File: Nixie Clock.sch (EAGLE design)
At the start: 46 parts, among them T0 MPSA42, T1 MPSA42, T10 MPSA42, T11 MPSA42, T12 MPSA42, T13 MPSA42, T14 MPSA42, T15 MPSA42, T16 MPSA42, T17 MPSA42, T18 MPSA42, T19 MPSA42, T2 MPSA42, T3 MPSA42, T4 MPSA42, T5 MPSA42, T6 MPSA42, T7 MPSA42, T8 MPSA42, T9 MPSA42

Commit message: Create 'Nixie Clock' and delete previous attempts with tubes
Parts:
- removed HOURS: (no value), con-harting:CON20
- removed HOURS_D, HOURS_U: IN-14, russian-nixies:IN-14
- removed POWER_SUPPLY: CON_2_SIL, PGT:CON_2_SIL
- added CON_LOGIC_POWER, CON_TUBE_POWER: CON_2_SIL, PGT:CON_2_SIL
- added HOURS_TENS, HOURS_UNITS, MINUTES_TENS, MINUTES_UNITS, SECONDS_TENS, SECONDS_UNITS: IN-14, russian-nixies:IN-14
- added R23, R24, R25, R26, R27, R28, R29, R30, R31, R32, R33, R34, R35, R36, R39, R40, R41, R42, R43, R44, R45, R46, R47, R48, R49, R50, R54: 33.3k, resistor:R-EU_0207/10
- added R37, R38: (no value), resistor:R-EU_0207/10
- added T20, T21, T22, T23, T24, T25, T26, T27, T28, T29, T30, T31, T32, T33, T34, T35, T36, T37, T38, T39, T40, T41, T42, T43, T44: MPSA42, PGT:MPSA42
- R10, R11, R12, R13, R14, R15, R16, R17, R18, R21, R22, R3, R4, R5, R6, R7, R8, R9: value (none) -> 33.3k
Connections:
- removed net DIGIT_D0: HOURS.10, R22.1
- removed net DIGIT_D1: HOURS.12, R13.1
- removed net DIGIT_D2: HOURS.14, R14.1
- removed net DIGIT_D3: HOURS.16, R15.1
- removed net DIGIT_D4: HOURS.18, R16.1
- removed net DIGIT_D5: HOURS.20, R17.1
- removed net DIGIT_D6: HOURS.2, R18.1
- removed net DIGIT_D7: HOURS.4, R19.1
- removed net DIGIT_D8: HOURS.6, R20.1
- removed net DIGIT_D9: HOURS.8, R21.1
- removed net DIGIT_U0: HOURS.9, R12.1
- removed net DIGIT_U1: HOURS.11, R3.1
- removed net DIGIT_U2: HOURS.13, R4.1
- removed net DIGIT_U3: HOURS.15, R5.1
- removed net DIGIT_U4: HOURS.17, R6.1
- removed net DIGIT_U5: HOURS.19, R7.1
- removed net DIGIT_U6: HOURS.1, R8.1
- removed net DIGIT_U7: HOURS.3, R9.1
- removed net DIGIT_U8: HOURS.5, R10.1
- removed net DIGIT_U9: HOURS.7, R11.1
- removed net N$1 (its old number): HOURS_U.0, T0.C
- removed net N$13 (its old number): HOURS_U.8, T8.C
- removed net N$14 (its old number): HOURS_U.7, T7.C
- removed net N$16 (its old number): HOURS_U.5, T5.C
- removed net N$17 (its old number): HOURS_U.1, T1.C
- removed net N$18 (its old number): HOURS_U.4, T4.C
- removed net N$2 (its old number): HOURS_U.9, T9.C
- new net N$33: SECONDS_UNITS.9, T9.C
- new net N$37: R26.2, T21.B
- new net N$38: R27.2, T22.B
- new net N$39: R28.2, T23.B
- new net N$40: R29.2, T24.B
- new net N$43: MINUTES_TENS.A, R20.1
- new net N$44: R31.2, T27.B
- new net N$45: R32.2, T28.B
- new net N$46: R33.2, T29.B
- new net N$47: R34.2, T30.B
- new net N$48: R35.2, T31.B
- new net N$49: R36.2, T26.B
- new net N$50: R21.2, T16.B
- new net N$51: R22.2, T17.B
- new net N$52: R23.2, T18.B
- new net N$53: MINUTES_TENS.1, T27.C
- new net N$54: MINUTES_TENS.2, T28.C
- new net N$55: MINUTES_TENS.3, T29.C
- new net N$56: MINUTES_TENS.4, T30.C
- new net N$57: MINUTES_TENS.5, T31.C
- new net N$58: MINUTES_TENS.0, T26.C
- new net N$59: MINUTES_UNITS.1, T16.C
- new net N$60: MINUTES_UNITS.2, T17.C
- new net N$61: MINUTES_UNITS.3, T18.C
- new net N$62: MINUTES_UNITS.4, T19.C
- new net N$63: MINUTES_UNITS.5, T20.C
- new net N$64: MINUTES_UNITS.6, T21.C
- new net N$65: MINUTES_UNITS.0, T25.C
- new net N$66: MINUTES_UNITS.9, T24.C
- new net N$67: MINUTES_UNITS.8, T23.C
- new net N$68: R43.2, T36.B
- new net N$69: R44.2, T37.B
- new net N$70: R45.2, T38.B
- new net N$71: R46.2, T39.B
- new net N$72: R47.2, T40.B
- new net N$73: R48.2, T41.B
- new net N$74: HOURS_UNITS.A, R37.1
- new net N$75: HOURS_TENS.A, R38.1
- new net N$76: R49.2, T43.B
- new net N$77: R50.2, T44.B
- new net N$78: HOURS_TENS.0, T42.C
- new net N$8: R1.1, SECONDS_UNITS.A
- new net N$81: R54.2, T42.B
- new net N$82: R39.2, T32.B
- new net N$83: R40.2, T33.B
- new net N$84: R41.2, T34.B
- new net N$85: HOURS_TENS.1, T43.C
- new net N$86: HOURS_TENS.2, T44.C
- new net N$9: R2.1, SECONDS_TENS.A
- new net N$91: HOURS_UNITS.1, T32.C
- new net N$92: HOURS_UNITS.2, T33.C
- new net N$93: HOURS_UNITS.3, T34.C
- new net N$94: HOURS_UNITS.4, T35.C
- new net N$95: HOURS_UNITS.5, T36.C
- new net N$96: HOURS_UNITS.6, T37.C
- new net N$97: HOURS_UNITS.0, T41.C
- new net N$98: HOURS_UNITS.9, T40.C
- new net N$99: HOURS_UNITS.8, T39.C
- new net VHIGH: CON_TUBE_POWER.P$1, R1.2, R19.2, R2.2, R20.2, R37.2, R38.2
- net GND: now also CON_LOGIC_POWER.P$2, CON_TUBE_POWER.P$2, HOURS_UNITS.7, MINUTES_UNITS.7, SECONDS_UNITS.7, T20.E, T21.E, T22.E, T23.E, T24.E, T25.E, T26.E, T27.E, T28.E, T29.E, T30.E, T31.E, T32.E, T33.E, T34.E, T35.E, T36.E, T37.E, T38.E, T39.E, T40.E, T41.E, T42.E, T43.E, T44.E; no longer POWER_SUPPLY.P$2
- net N$15: now also R18.2, T10.B; no longer HOURS_U.6, T6.C
- net N$19: now also SECONDS_TENS.1, T11.C; no longer HOURS_U.2, T2.C
- net N$20: now also SECONDS_TENS.2, T12.C; no longer HOURS_D.0, T10.C
- net N$21: now also SECONDS_TENS.3, T13.C; no longer HOURS_U.3, T3.C
- net N$22: now also SECONDS_TENS.4, T14.C; no longer HOURS_D.9, T19.C
- net N$23: now also SECONDS_TENS.5, T15.C; no longer HOURS_U.A, R1.2
- net N$24: now also SECONDS_TENS.0, T10.C; no longer HOURS_D.8, T18.C
- net N$25: now also R42.2, T35.B; no longer HOURS_D.7, T17.C
- net N$26: now also SECONDS_UNITS.1, T1.C; no longer HOURS_D.6, T16.C
- net N$27: now also SECONDS_UNITS.2, T2.C; no longer HOURS_D.5, T15.C
- net N$28: now also SECONDS_UNITS.3, T3.C; no longer HOURS_D.2, T12.C
- net N$29: now also SECONDS_UNITS.4, T4.C; no longer HOURS_D.A, R2.2
- net N$30: now also SECONDS_UNITS.5, T5.C; no longer HOURS_D.3, T13.C
- net N$31: now also SECONDS_UNITS.6, T6.C; no longer HOURS_D.4, T14.C
- net N$32: now also SECONDS_UNITS.0, T0.C; no longer HOURS_D.1, T11.C
- net N$34: now also SECONDS_UNITS.8, T8.C; no longer R18.2, T16.B
- net N$35: now also R24.2, T19.B; no longer R19.2, T17.B
- net N$36: now also R25.2, T20.B; no longer R22.2, T10.B
- net N$41: now also R30.2, T25.B; no longer R20.2, T18.B
- net N$42: now also MINUTES_UNITS.A, R19.1; no longer R21.2, T19.B
- net VCC: now also CON_LOGIC_POWER.P$1; no longer POWER_SUPPLY.P$1, R1.1, R2.1

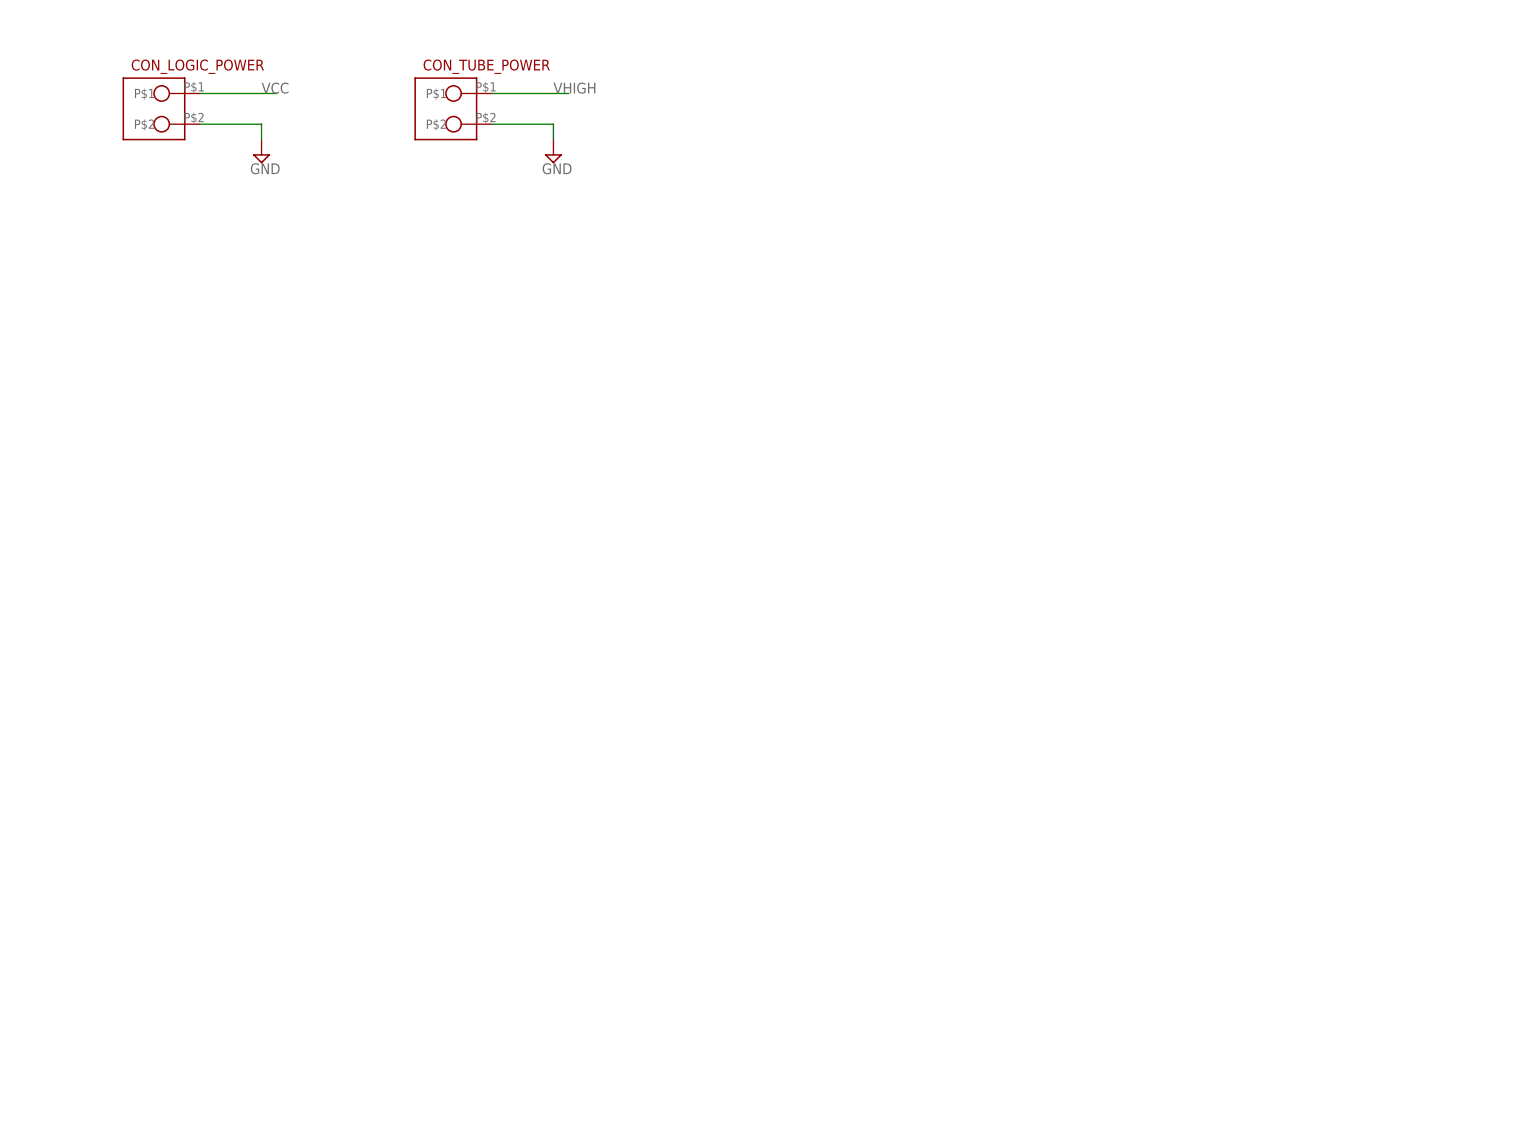
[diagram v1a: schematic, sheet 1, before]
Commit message: Uncompleted schematics for the Nixie Clock and simulation for AND with diodes
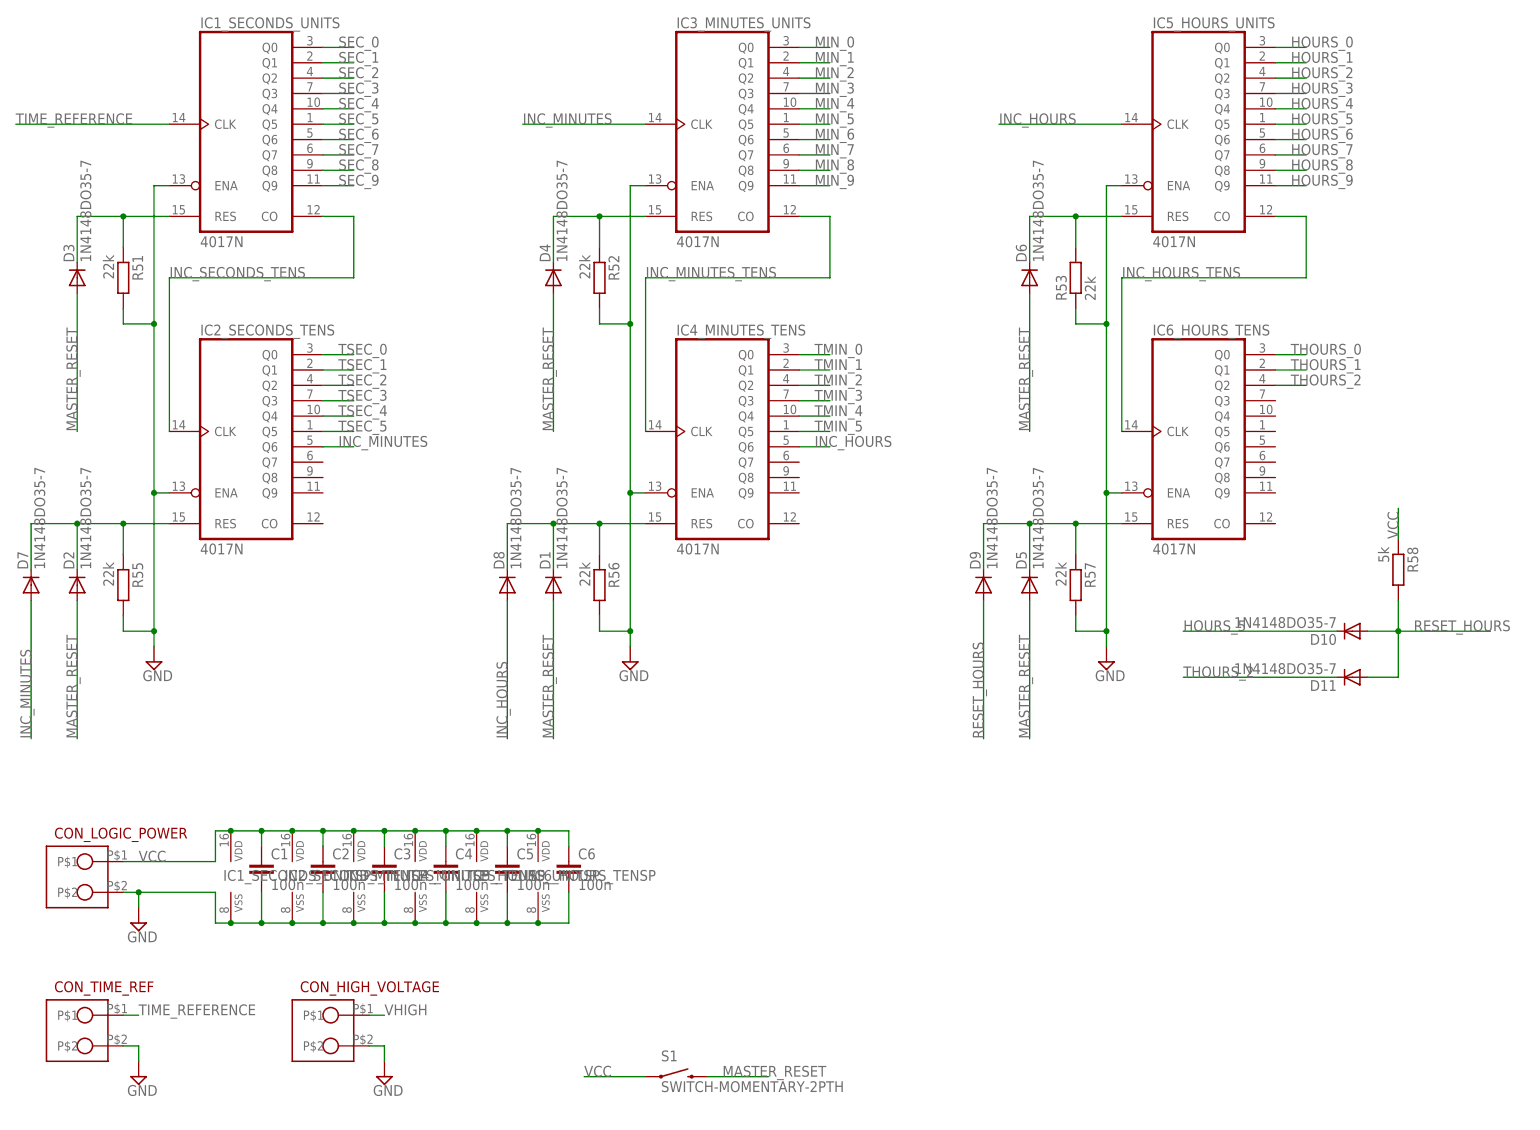
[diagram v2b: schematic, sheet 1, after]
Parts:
- removed CON_TUBE_POWER: CON_2_SIL, PGT:CON_2_SIL
- added C1, C2, C3, C4, C5, C6: 100n, resistor:C-EU050-030X075
- added CON_HIGH_VOLTAGE, CON_TIME_REF: CON_2_SIL, PGT:CON_2_SIL
- added D1, D10, D11, D2, D3, D4, D5, D6, D7, D8, D9: 1N4148DO35-7, diode:1N4148DO35-7
- added IC1_SECONDS_UNITS, IC2_SECONDS_TENS, IC3_MINUTES_UNITS, IC4_MINUTES_TENS, IC5_HOURS_UNITS, IC6_HOURS_TENS: 4017N, 40xx:4017N
- added R51, R52, R53, R55, R56, R57: 22k, resistor:R-EU_0207/10
- added R58: 5k, resistor:R-EU_0207/10
- added S1: SWITCH-MOMENTARY-2PTH, SparkFun-Electromechanical:SWITCH-MOMENTARY-2PTH
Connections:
- new net HOURS_0: IC5_HOURS_UNITSA.Q0, R48.1
- new net HOURS_1: IC5_HOURS_UNITSA.Q1, R39.1
- new net HOURS_2: IC5_HOURS_UNITSA.Q2, R40.1
- new net HOURS_3: IC5_HOURS_UNITSA.Q3, R41.1
- new net HOURS_4: IC5_HOURS_UNITSA.Q4, R42.1
- new net HOURS_5: D10.C, IC5_HOURS_UNITSA.Q5, R43.1
- new net HOURS_6: IC5_HOURS_UNITSA.Q6, R44.1
- new net HOURS_7: IC5_HOURS_UNITSA.Q7, R45.1
- new net HOURS_8: IC5_HOURS_UNITSA.Q8, R46.1
- new net HOURS_9: IC5_HOURS_UNITSA.Q9, R47.1
- new net INC_HOURS: D8.A, IC4_MINUTES_TENSA.Q6, IC5_HOURS_UNITSA.CLK
- new net INC_HOURS_TENS: IC5_HOURS_UNITSA.CO, IC6_HOURS_TENSA.CLK
- new net INC_MINUTES: D7.A, IC2_SECONDS_TENSA.Q6, IC3_MINUTES_UNITSA.CLK
- new net INC_MINUTES_TENS: IC3_MINUTES_UNITSA.CO, IC4_MINUTES_TENSA.CLK
- new net INC_SECONDS_TENS: IC1_SECONDS_UNITSA.CO, IC2_SECONDS_TENSA.CLK
- new net MASTER_RESET: D1.A, D2.A, D3.A, D4.A, D5.A, D6.A, S1.2
- new net MIN_0: IC3_MINUTES_UNITSA.Q0, R30.1
- new net MIN_1: IC3_MINUTES_UNITSA.Q1, R21.1
- new net MIN_2: IC3_MINUTES_UNITSA.Q2, R22.1
- new net MIN_3: IC3_MINUTES_UNITSA.Q3, R23.1
- new net MIN_4: IC3_MINUTES_UNITSA.Q4, R24.1
- new net MIN_5: IC3_MINUTES_UNITSA.Q5, R25.1
- new net MIN_6: IC3_MINUTES_UNITSA.Q6, R26.1
- new net MIN_7: IC3_MINUTES_UNITSA.Q7, R27.1
- new net MIN_8: IC3_MINUTES_UNITSA.Q8, R28.1
- new net MIN_9: IC3_MINUTES_UNITSA.Q9, R29.1
- new net N$100: D1.C, D8.C, IC4_MINUTES_TENSA.RES, R56.1
- new net N$102: D4.C, IC3_MINUTES_UNITSA.RES, R52.1
- new net N$104: D5.C, D9.C, IC6_HOURS_TENSA.RES, R57.1
- new net N$106: D6.C, IC5_HOURS_UNITSA.RES, R53.2
- new net N$79: SECONDS_UNITS.7, T7.C
- new net N$80: D2.C, D7.C, IC2_SECONDS_TENSA.RES, R55.1
- new net N$87: MINUTES_UNITS.7, T22.C
- new net N$88: HOURS_UNITS.7, T38.C
- new net N$89: D3.C, IC1_SECONDS_UNITSA.RES, R51.1
- new net RESET_HOURS: D10.A, D11.A, D9.A, R58.2
- new net SEC_0: IC1_SECONDS_UNITSA.Q0, R12.1
- new net SEC_1: IC1_SECONDS_UNITSA.Q1, R3.1
- new net SEC_2: IC1_SECONDS_UNITSA.Q2, R4.1
- new net SEC_3: IC1_SECONDS_UNITSA.Q3, R5.1
- new net SEC_4: IC1_SECONDS_UNITSA.Q4, R6.1
- new net SEC_5: IC1_SECONDS_UNITSA.Q5, R7.1
- new net SEC_6: IC1_SECONDS_UNITSA.Q6, R8.1
- new net SEC_7: IC1_SECONDS_UNITSA.Q7, R9.1
- new net SEC_8: IC1_SECONDS_UNITSA.Q8, R10.1
- new net SEC_9: IC1_SECONDS_UNITSA.Q9, R11.1
- new net THOURS_0: IC6_HOURS_TENSA.Q0, R54.1
- new net THOURS_1: IC6_HOURS_TENSA.Q1, R49.1
- new net THOURS_2: D11.C, IC6_HOURS_TENSA.Q2, R50.1
- new net TIME_REFERENCE: CON_TIME_REF.P$1, IC1_SECONDS_UNITSA.CLK
- new net TMIN_0: IC4_MINUTES_TENSA.Q0, R36.1
- new net TMIN_1: IC4_MINUTES_TENSA.Q1, R31.1
- new net TMIN_2: IC4_MINUTES_TENSA.Q2, R32.1
- new net TMIN_3: IC4_MINUTES_TENSA.Q3, R33.1
- new net TMIN_4: IC4_MINUTES_TENSA.Q4, R34.1
- new net TMIN_5: IC4_MINUTES_TENSA.Q5, R35.1
- new net TSEC_0: IC2_SECONDS_TENSA.Q0, R18.1
- new net TSEC_1: IC2_SECONDS_TENSA.Q1, R13.1
- new net TSEC_2: IC2_SECONDS_TENSA.Q2, R14.1
- new net TSEC_3: IC2_SECONDS_TENSA.Q3, R15.1
- new net TSEC_4: IC2_SECONDS_TENSA.Q4, R16.1
- new net TSEC_5: IC2_SECONDS_TENSA.Q5, R17.1
- net GND: now also C1.2, C2.2, C3.2, C4.2, C5.2, C6.2, CON_HIGH_VOLTAGE.P$2, CON_TIME_REF.P$2, IC1_SECONDS_UNITSA.ENA, IC1_SECONDS_UNITSP.VSS, IC2_SECONDS_TENSA.ENA, IC2_SECONDS_TENSP.VSS, IC3_MINUTES_UNITSA.ENA, IC3_MINUTES_UNITSP.VSS, IC4_MINUTES_TENSA.ENA, IC4_MINUTES_TENSP.VSS, IC5_HOURS_UNITSA.ENA, IC5_HOURS_UNITSP.VSS, IC6_HOURS_TENSA.ENA, IC6_HOURS_TENSP.VSS, R51.2, R52.2, R53.1, R55.2, R56.2, R57.2; no longer CON_TUBE_POWER.P$2, HOURS_UNITS.7, MINUTES_UNITS.7, SECONDS_UNITS.7
- net VCC: now also C1.1, C2.1, C3.1, C4.1, C5.1, C6.1, IC1_SECONDS_UNITSP.VDD, IC2_SECONDS_TENSP.VDD, IC3_MINUTES_UNITSP.VDD, IC4_MINUTES_TENSP.VDD, IC5_HOURS_UNITSP.VDD, IC6_HOURS_TENSP.VDD, R58.1, S1.1
- net VHIGH: now also CON_HIGH_VOLTAGE.P$1; no longer CON_TUBE_POWER.P$1
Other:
- moved on the sheet: CON_LOGIC_POWER

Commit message: Fix MSPA42 and IN-14 packages
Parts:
- HOURS_TENS, HOURS_UNITS, MINUTES_TENS, MINUTES_UNITS, SECONDS_TENS, SECONDS_UNITS: device russian-nixies:IN-14 -> PGT:IN-14
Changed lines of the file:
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@@
 <parts>
 <part name="FRAME1" library="frames" deviceset="LETTER_L" device="" value="TUBES_FOR_SECONDS"/>
-<part name="SECONDS_UNITS" library="russian-nixies" deviceset="IN-14" device=""/>
-<part name="SECONDS_TENS" library="russian-nixies" deviceset="IN-14" device=""/>
+<part name="SECONDS_UNITS" library="PGT" deviceset="IN-14" device=""/>
+<part name="SECONDS_TENS" library="PGT" deviceset="IN-14" device=""/>
 <part name="T1" library="PGT" deviceset="MPSA42" device=""/>
 <part name="T2" library="PGT" deviceset="MPSA42" device=""/>
@@
 <part name="SUPPLY4" library="supply2" deviceset="GND" device=""/>
 <part name="FRAME2" library="frames" deviceset="LETTER_L" device="" value="TUBES_FOR_MINUTES"/>
-<part name="MINUTES_UNITS" library="russian-nixies" deviceset="IN-14" device=""/>
-<part name="MINUTES_TENS" library="russian-nixies" deviceset="IN-14" device=""/>
+<part name="MINUTES_UNITS" library="PGT" deviceset="IN-14" device=""/>
+<part name="MINUTES_TENS" library="PGT" deviceset="IN-14" device=""/>
 <part name="T16" library="PGT" deviceset="MPSA42" device=""/>
 <part name="T17" library="PGT" deviceset="MPSA42" device=""/>
@@
 <part name="SUPPLY8" library="supply2" deviceset="GND" device=""/>
 <part name="FRAME3" library="frames" deviceset="LETTER_L" device="" value="TUBES_FOR_HOURS"/>
-<part name="HOURS_UNITS" library="russian-nixies" deviceset="IN-14" device=""/>
-<part name="HOURS_TENS" library="russian-nixies" deviceset="IN-14" device=""/>
+<part name="HOURS_UNITS" library="PGT" deviceset="IN-14" device=""/>
+<part name="HOURS_TENS" library="PGT" deviceset="IN-14" device=""/>
 <part name="T32" library="PGT" deviceset="MPSA42" device=""/>
 <part name="T33" library="PGT" deviceset="MPSA42" device=""/>
 <part name="T34" library="PGT" deviceset="MPSA42" device=""/>
 <part name="T35" library="PGT" deviceset="MPSA42" device=""/>
-<part name="T36" library="PGT" deviceset="MPSA42" device=""/>
 <part name="T37" library="PGT" deviceset="MPSA42" device=""/>
 <part name="T38" library="PGT" deviceset="MPSA42" device=""/>
@@
 <part name="C5" library="resistor" deviceset="C-EU" device="050-030X075" value="100n"/>
 <part name="C6" library="resistor" deviceset="C-EU" device="050-030X075" value="100n"/>
+<part name="T36" library="PGT" deviceset="MPSA42" device=""/>
 </parts>
 <sheets>
@@
 <instance part="T34" gate="G$1" x="43.18" y="132.08"/>
 <instance part="T35" gate="G$1" x="43.18" y="116.84"/>
-<instance part="T36" gate="G$1" x="43.18" y="101.6"/>
 <instance part="T37" gate="G$1" x="43.18" y="86.36"/>
 <instance part="T38" gate="G$1" x="43.18" y="71.12"/>
@@
 <instance part="SUPPLY11" gate="GND" x="50.8" y="12.7"/>
 <instance part="SUPPLY12" gate="GND" x="180.34" y="78.74"/>
+<instance part="T36" gate="G$1" x="43.18" y="101.6"/>
 </instances>
 <busses>
@@
 <segment>
 <pinref part="R43" gate="G$1" pin="2"/>
+<wire x1="38.1" y1="101.6" x2="40.64" y2="101.6" width="0.1524" layer="91"/>
 <pinref part="T36" gate="G$1" pin="B"/>
-<wire x1="38.1" y1="101.6" x2="40.64" y2="101.6" width="0.1524" layer="91"/>
 </segment>
 </net>
@@
 <wire x1="50.8" y1="81.28" x2="50.8" y2="66.04" width="0.1524" layer="91"/>
 <junction x="50.8" y="66.04"/>
-<pinref part="T36" gate="G$1" pin="E"/>
 <wire x1="45.72" y1="96.52" x2="50.8" y2="96.52" width="0.1524" layer="91"/>
 <wire x1="50.8" y1="96.52" x2="50.8" y2="81.28" width="0.1524" layer="91"/>
@@
 <wire x1="50.8" y1="157.48" x2="50.8" y2="142.24" width="0.1524" layer="91"/>
 <junction x="50.8" y="142.24"/>
+<pinref part="T36" gate="G$1" pin="E"/>
 </segment>
 </net>
@@
 <net name="N$95" class="0">
 <segment>
-<pinref part="T36" gate="G$1" pin="C"/>
 <wire x1="45.72" y1="106.68" x2="60.96" y2="106.68" width="0.1524" layer="91"/>
 <wire x1="60.96" y1="106.68" x2="60.96" y2="93.98" width="0.1524" layer="91"/>
 <pinref part="HOURS_UNITS" gate="G$1" pin="5"/>
 <wire x1="60.96" y1="93.98" x2="73.66" y2="93.98" width="0.1524" layer="91"/>
-</segment>
-</net>
+<pinref part="T36" gate="G$1" pin="C"/>
+</segment>
+</net>
